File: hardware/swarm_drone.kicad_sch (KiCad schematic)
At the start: 0 parts

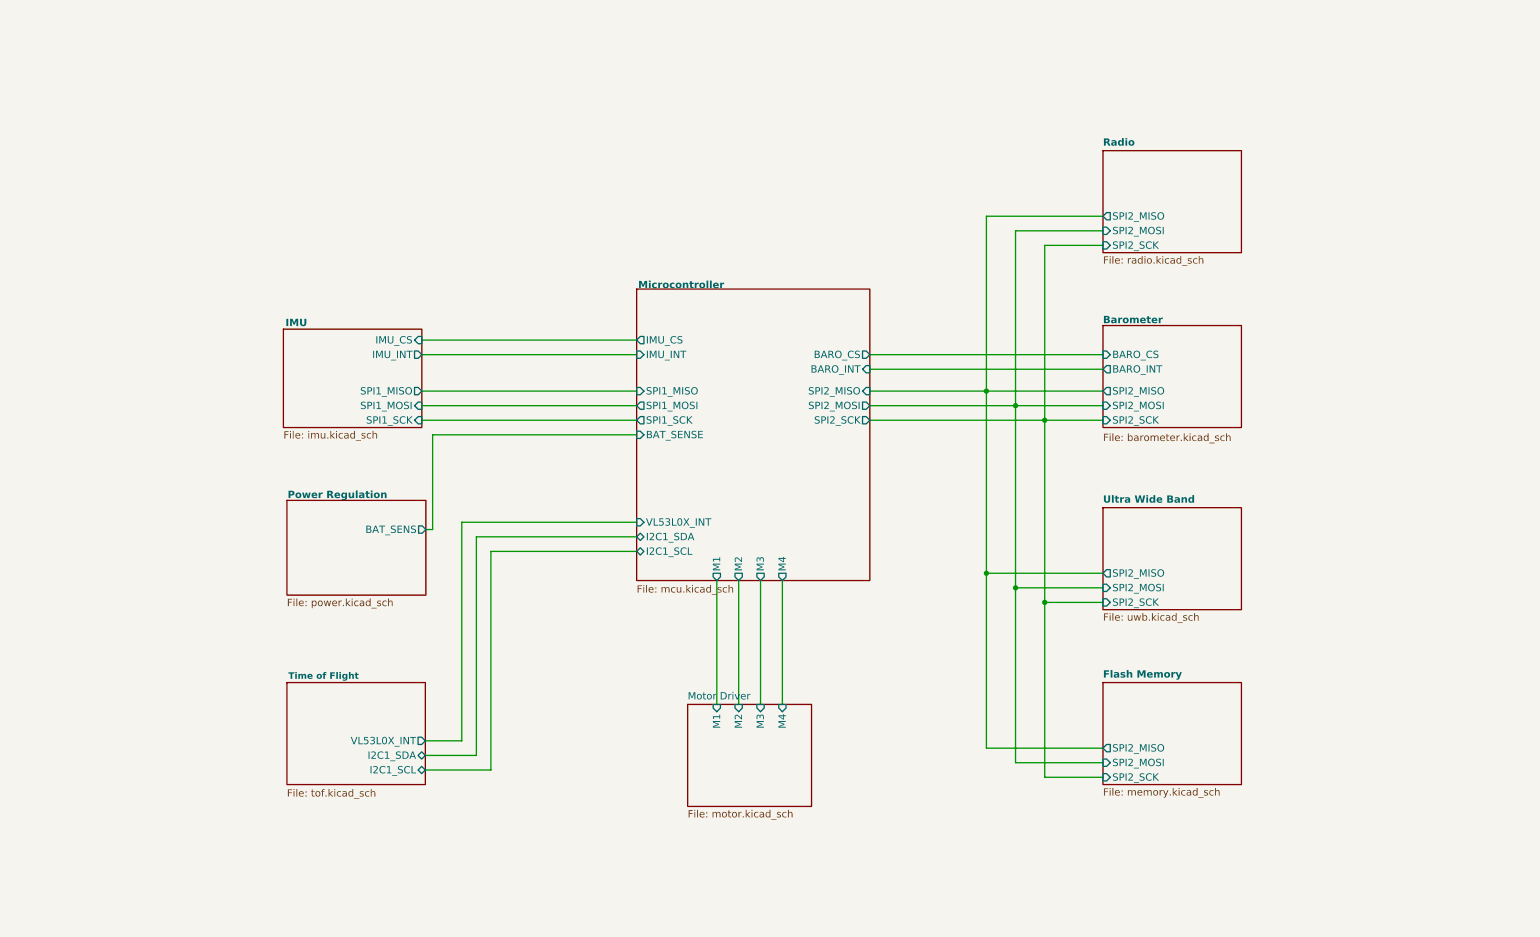
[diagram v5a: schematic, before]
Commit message: feat(kicad): Added several open sourced footprint libraries, finished schematic design for nrf, uwb, tof, flash, motors and added all reference material to refs folder
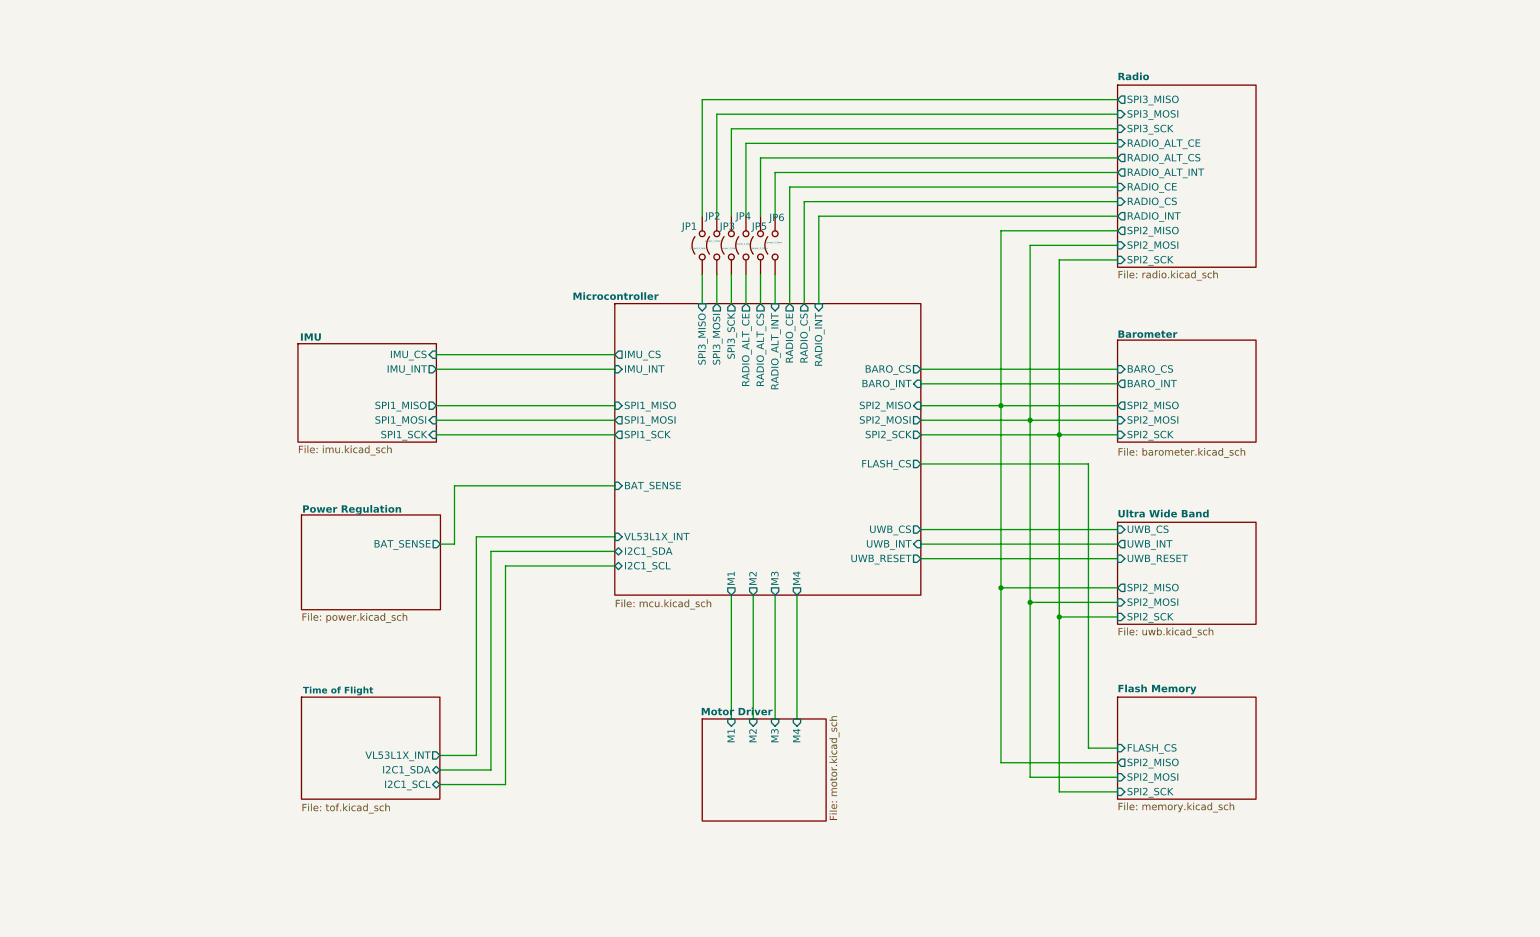
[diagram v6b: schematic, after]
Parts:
- added JP1, JP2, JP3, JP4, JP5, JP6: Jumper_2_Open, Jumper:SolderJumper-2_P1.3mm_Open_RoundedPad1.0x1.5mm, symbol Jumper:Jumper_2_Open
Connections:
- new net Microcontroller/RADIO_ALT_CE: JP4.1 (A)
- new net Microcontroller/RADIO_ALT_CS: JP5.1 (A)
- new net Microcontroller/RADIO_ALT_INT: JP6.1 (A)
- new net Microcontroller/SPI3_MISO: JP1.1 (A)
- new net Microcontroller/SPI3_MOSI: JP2.1 (A)
- new net Microcontroller/SPI3_SCK: JP3.1 (A)
- new net Radio/RADIO_ALT_CE: JP4.2 (B)
- new net Radio/RADIO_ALT_CS: JP5.2 (B)
- new net Radio/RADIO_ALT_INT: JP6.2 (B)
- new net Radio/SPI3_MISO: JP1.2 (B)
- new net Radio/SPI3_MOSI: JP2.2 (B)
- new net Radio/SPI3_SCK: JP3.2 (B)
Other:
- sheet Flash Memory ports: added FLASH_CS; removed none
- sheet Microcontroller ports: added FLASH_CS, RADIO_ALT_CE, RADIO_ALT_CS, RADIO_ALT_INT, RADIO_CE, RADIO_CS, RADIO_INT, SPI3_MISO, SPI3_MOSI, SPI3_SCK, UWB_CS, UWB_INT, UWB_RESET, VL53L1X_INT; removed VL53L0X_INT
- sheet Power Regulation ports: added BAT_SENSE; removed BAT_SENS
- sheet Radio ports: added RADIO_ALT_CE, RADIO_ALT_CS, RADIO_ALT_INT, RADIO_CE, RADIO_CS, RADIO_INT, SPI3_MISO, SPI3_MOSI, SPI3_SCK; removed none
- sheet Time of Flight ports: added VL53L1X_INT; removed VL53L0X_INT
- sheet Ultra Wide Band ports: added UWB_CS, UWB_INT, UWB_RESET; removed none

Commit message: feat(kicad): Finished initial draft of the schematic design All pinouts are set
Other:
- note added: "HIGH LEVEL BLOCK DIAGRAM"
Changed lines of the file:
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@@
 	(generator_version "10.0")
 	(paper "A4")
+	(rectangle
+		(start 59.69 20.32)
+		(end 238.76 162.56)
+		(stroke
+			(width 0.508)
+			(type solid)
+		)
+		(fill
+			(type none)
+		)
+	)
+	(text "HIGH LEVEL BLOCK DIAGRAM\n"
+		(exclude_from_sim no)
+		(at 224.028 160.782 0)
+		(effects
+			(font
+				(size 1.27 1.27)
+			)
+		)
+	)
 	(junction
 		(at 193.04 118.11)
@@
 	(wire
 		(pts
-			(xy 135.89 66.04) (xy 135.89 60.96)
+			(xy 135.89 62.23) (xy 135.89 60.96)
 		)
 		(stroke
@@
 	(wire
 		(pts
-			(xy 148.59 116.84) (xy 148.59 138.43)
-		)
-		(stroke
-			(width 0)
-			(type default)
-		)
-	)
-	(wire
-		(pts
-			(xy 143.51 66.04) (xy 143.51 60.96)
+			(xy 148.59 116.84) (xy 148.59 134.62)
+		)
+		(stroke
+			(width 0)
+			(type default)
+		)
+	)
+	(wire
+		(pts
+			(xy 143.51 62.23) (xy 143.51 60.96)
 		)
 		(stroke
@@
 	(wire
 		(pts
-			(xy 148.59 66.04) (xy 148.59 60.96)
+			(xy 148.59 62.23) (xy 148.59 60.96)
 		)
 		(stroke
@@
 	(wire
 		(pts
-			(xy 146.05 66.04) (xy 146.05 60.96)
+			(xy 146.05 62.23) (xy 146.05 60.96)
 		)
 		(stroke
@@
 	(wire
 		(pts
-			(xy 144.78 116.84) (xy 144.78 138.43)
-		)
-		(stroke
-			(width 0)
-			(type default)
-		)
-	)
-	(wire
-		(pts
-			(xy 152.4 116.84) (xy 152.4 138.43)
+			(xy 144.78 116.84) (xy 144.78 134.62)
+		)
+		(stroke
+			(width 0)
+			(type default)
+		)
+	)
+	(wire
+		(pts
+			(xy 152.4 116.84) (xy 152.4 134.62)
 		)
 		(stroke
@@
 	(wire
 		(pts
-			(xy 156.21 66.04) (xy 156.21 50.8)
+			(xy 156.21 62.23) (xy 156.21 50.8)
 		)
 		(stroke
@@
 	(wire
 		(pts
-			(xy 151.13 66.04) (xy 151.13 45.72)
+			(xy 151.13 62.23) (xy 151.13 45.72)
 		)
 		(stroke
@@
 	(wire
 		(pts
-			(xy 153.67 66.04) (xy 153.67 48.26)
+			(xy 153.67 62.23) (xy 153.67 48.26)
 		)
 		(stroke
@@
 	(wire
 		(pts
-			(xy 140.97 116.84) (xy 140.97 138.43)
-		)
-		(stroke
-			(width 0)
-			(type default)
-		)
-	)
-	(wire
-		(pts
-			(xy 140.97 66.04) (xy 140.97 60.96)
+			(xy 140.97 116.84) (xy 140.97 134.62)
+		)
+		(stroke
+			(width 0)
+			(type default)
+		)
+	)
+	(wire
+		(pts
+			(xy 140.97 62.23) (xy 140.97 60.96)
 		)
 		(stroke
@@
 	(wire
 		(pts
-			(xy 138.43 66.04) (xy 138.43 60.96)
+			(xy 138.43 62.23) (xy 138.43 60.96)
 		)
 		(stroke
@@
 	)
 	(sheet
-		(at 120.65 66.04)
-		(size 53.34 50.8)
+		(at 120.65 62.23)
+		(size 53.34 54.61)
 		(exclude_from_sim no)
 		(in_bom yes)
@@
 		)
 		(property "Sheetname" "Microcontroller"
-			(at 113.284 65.532 0)
+			(at 120.65 61.976 0)
 			(show_name no)
 			(do_not_autoplace no)
@@
 		)
 		(property "Sheetfile" "mcu.kicad_sch"
-			(at 120.65 117.602 0)
+			(at 120.65 113.792 0)
 			(show_name no)
 			(do_not_autoplace no)
@@
 		)
 		(pin "SPI3_MISO" input
-			(at 135.89 66.04 90)
+			(at 135.89 62.23 90)
 			(effects
 				(font
@@
 		)
 		(pin "SPI3_MOSI" output
-			(at 138.43 66.04 90)
+			(at 138.43 62.23 90)
 			(effects
 				(font
@@
 		)
 		(pin "SPI3_SCK" output
-			(at 140.97 66.04 90)
+			(at 140.97 62.23 90)
 			(effects
 				(font
@@
 		)
 		(pin "RADIO_ALT_CE" output
-			(at 143.51 66.04 90)
+			(at 143.51 62.23 90)
 			(effects
 				(font
@@
 		)
 		(pin "RADIO_ALT_CS" output
-			(at 146.05 66.04 90)
+			(at 146.05 62.23 90)
 			(effects
 				(font
@@
 		)
 		(pin "RADIO_ALT_INT" input
-			(at 148.59 66.04 90)
+			(at 148.59 62.23 90)
 			(effects
 				(font
@@
 		)
 		(pin "RADIO_CE" output
-			(at 151.13 66.04 90)
+			(at 151.13 62.23 90)
 			(effects
 				(font
@@
 		)
 		(pin "RADIO_CS" output
-			(at 153.67 66.04 90)
+			(at 153.67 62.23 90)
 			(effects
 				(font
@@
 		)
 		(pin "RADIO_INT" input
-			(at 156.21 66.04 90)
+			(at 156.21 62.23 90)
 			(effects
 				(font
@@
 		(on_board yes)
 		(dnp no)
-		(fields_autoplaced yes)
 		(stroke
 			(width 0.1524)
@@
 		)
 		(property "Sheetname" "Flash Memory"
-			(at 208.28 133.9084 0)
+			(at 208.28 134.366 0)
 			(show_name no)
 			(do_not_autoplace no)
@@
 	)
 	(sheet
-		(at 135.89 138.43)
+		(at 135.89 134.62)
 		(size 21.59 17.78)
 		(exclude_from_sim no)
@@
 		)
 		(property "Sheetname" "Motor Driver"
-			(at 135.636 137.922 0)
+			(at 135.636 134.112 0)
 			(show_name no)
 			(do_not_autoplace no)
@@
 		)
 		(property "Sheetfile" "motor.kicad_sch"
-			(at 158.0646 156.21 90)
+			(at 135.636 153.416 0)
 			(show_name no)
 			(do_not_autoplace no)
@@
 		)
 		(pin "M1" input
-			(at 140.97 138.43 90)
+			(at 140.97 134.62 90)
 			(effects
 				(font
@@
 		)
 		(pin "M2" input
-			(at 144.78 138.43 90)
+			(at 144.78 134.62 90)
 			(effects
 				(font
@@
 		)
 		(pin "M3" input
-			(at 148.59 138.43 90)
+			(at 148.59 134.62 90)
 			(effects
 				(font
@@
 		)
 		(pin "M4" input
-			(at 152.4 138.43 90)
-			(effects
-				(font
+			(at 152.4 134.62 90)
+			(effects
+				(font
